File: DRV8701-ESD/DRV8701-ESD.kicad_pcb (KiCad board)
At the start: 4 copper layers, 55 x 95 mm, 78 parts, among them J1 V_Main, J10 POT_signal, J11 GND, J12 Conn_01x05_Pin, J13 CW, J14 CW, J15 CW, J17 CW, J18 CW, J19 CW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

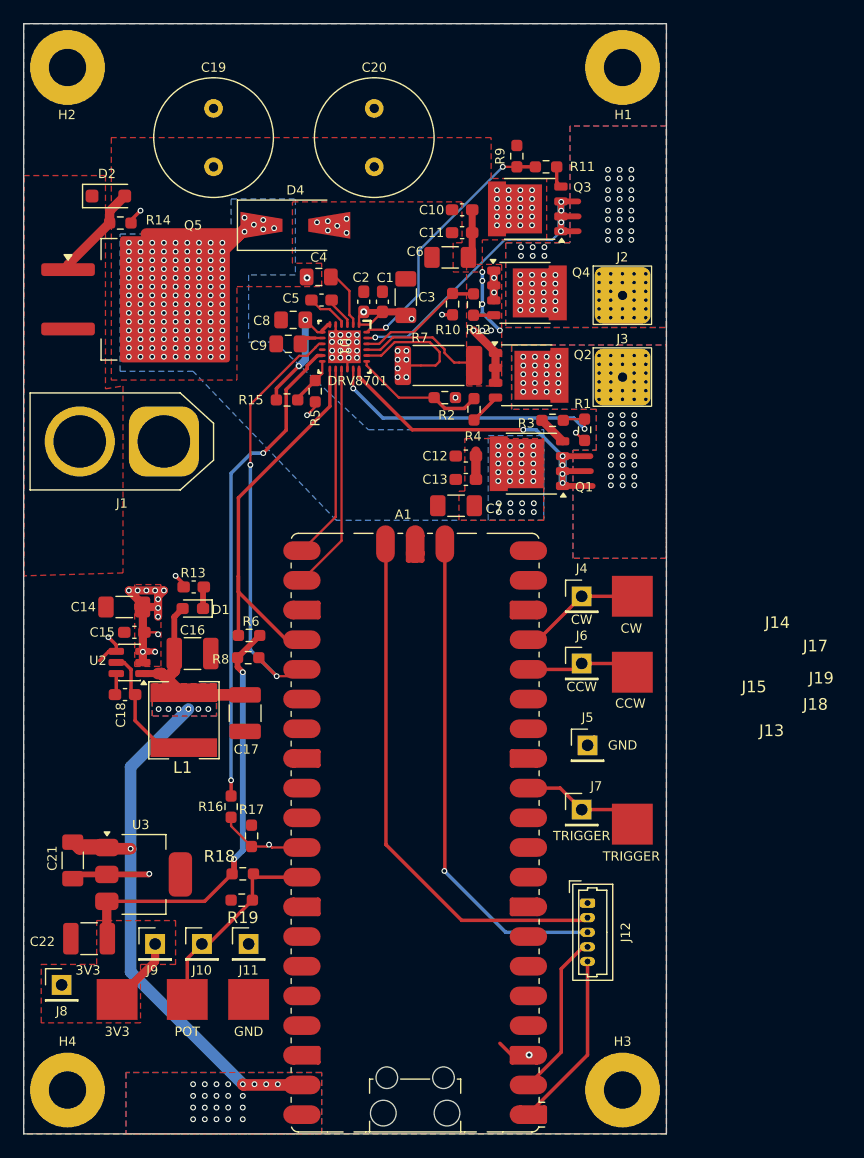
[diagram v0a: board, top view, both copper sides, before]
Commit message: Added SMD and THT Debug Connectors. Some small changes.
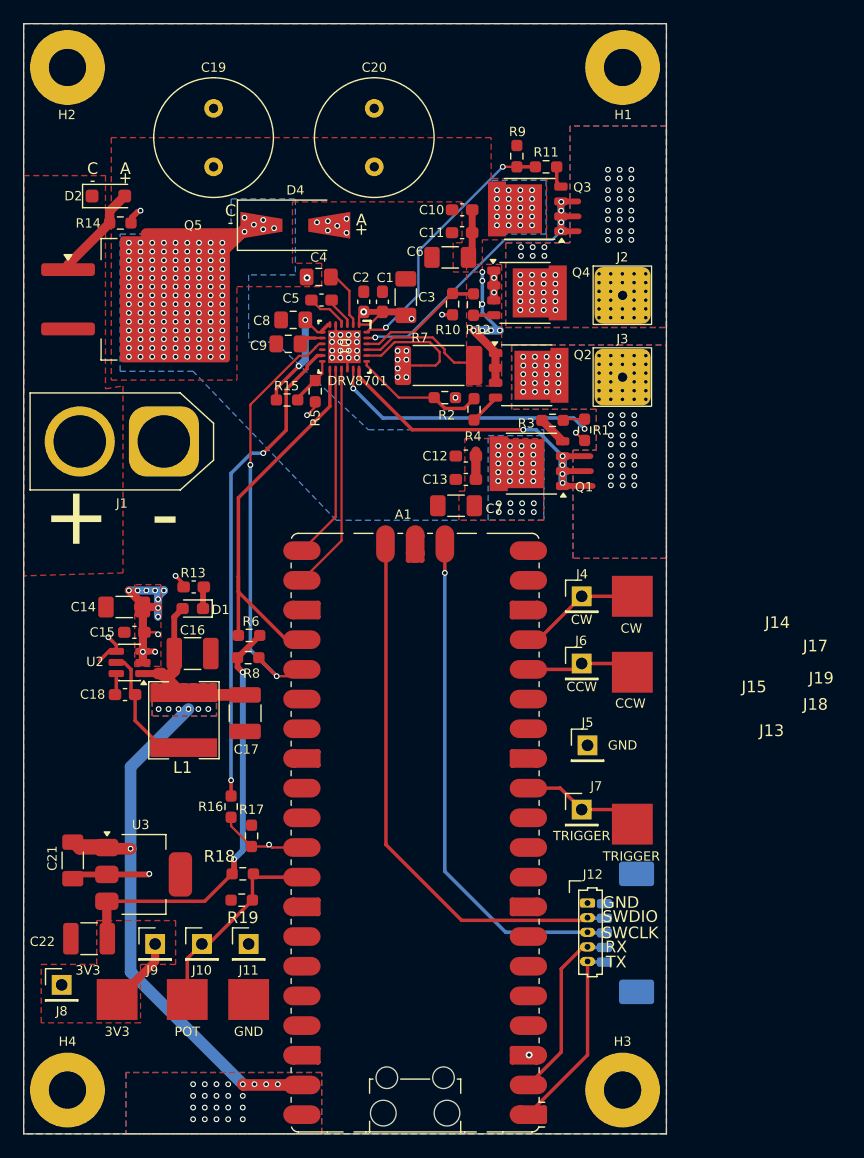
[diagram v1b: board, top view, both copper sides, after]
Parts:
- added J16: Conn_01x05_Pin, Connector_Molex:Molex_PicoBlade_53398-0571_1x05-1MP_P1.25mm_Vertical, B.Cu at (174.4, 122.8)
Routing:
- net /SP_TOP: track 14.1 -> 16.4 mm
- net /DEBUG_RX: track 14.1 -> 15.6 mm
- net /DEBUG_TX: track 15.2 -> 16.7 mm
- net /SWDIO: track 45.0 -> 46.4 mm
- net /SWCLK: track 41.6 -> 43.1 mm
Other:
- board text added: "+"
- board text added: "-"
- board text added: "A"
- board text added: "C"
- board text added: "RX"
- board text added: "SWCLK"
- board text added: "SWDIO"
- board text added: "TX"
